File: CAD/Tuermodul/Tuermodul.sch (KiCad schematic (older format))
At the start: 45 parts, among them J101 Conn_02x16_Counter_Clockwise, U101 93LC46B, U102 74HC595, U103 FT4232H, U104 MCP1825S, Y101 12MHz

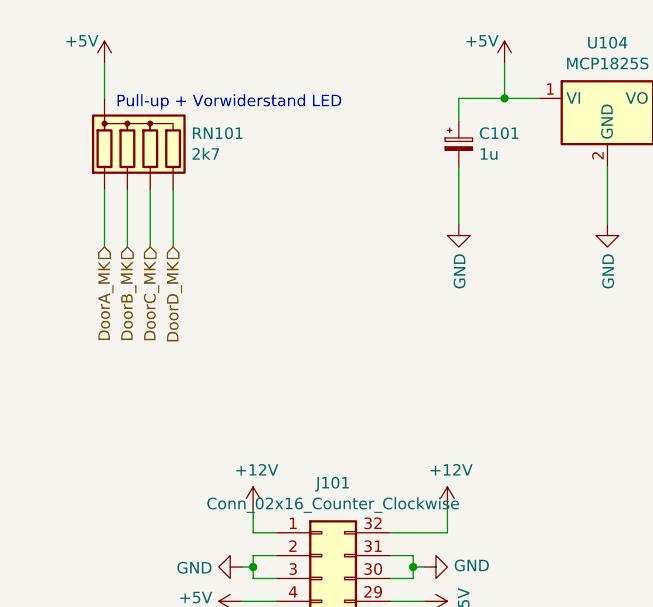
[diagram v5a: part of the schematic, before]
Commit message: -mod: Umbelegung Stecker zwischen Haupt und Frontplatine -add: 100n caps für MK Entprellung -mod: Routing Stecker -mod: Platzierung Front nach Vorgabe
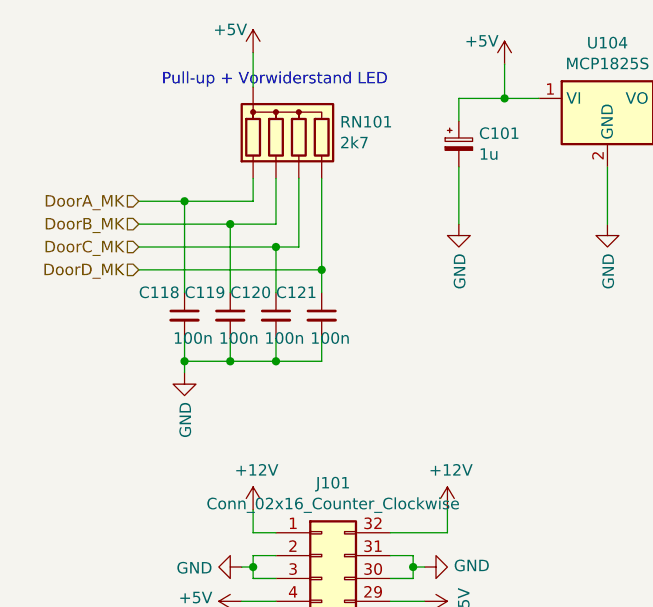
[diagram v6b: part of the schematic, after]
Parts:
- added C118, C119, C120, C121: 100n, Capacitor_SMD:C_0603_1608Metric_Pad1.05x0.95mm_HandSolder, symbol Device:C_Small
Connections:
- net DoorA_MK: now also C118.1
- net DoorB_MK: now also C119.1
- net DoorC_MK: now also C120.1
- net DoorD_MK: now also C121.1
- net GND: now also C118.2, C119.2, C120.2, C121.2
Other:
- moved on the sheet: RN101
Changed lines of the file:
@@
 Wire Wire Line
 	8500 3750 8150 3750
-Text HLabel 800  1450 3    50   Input ~ 0
+Text HLabel 950  1250 0    50   Input ~ 0
 DoorA_MK
-Text HLabel 900  1450 3    50   Input ~ 0
+Text HLabel 950  1350 0    50   Input ~ 0
 DoorB_MK
-Text HLabel 1000 1450 3    50   Input ~ 0
+Text HLabel 950  1450 0    50   Input ~ 0
 DoorC_MK
-Text HLabel 1100 1450 3    50   Input ~ 0
+Text HLabel 950  1550 0    50   Input ~ 0
 DoorD_MK
 $Comp
 L Device:R_Network04 RN101
 U 1 1 5C769116
-P 1000 1000
-F 0 "RN101" H 1180 1046 50  0000 L CNN
-F 1 "2k7" H 1180 955 50  0000 L CNN
-F 2 "Resistor_THT:R_Array_SIP5" V 1275 1000 50  0001 C CNN
-F 3 "http://www.vishay.com/docs/31509/csc.pdf" H 1000 1000 50  0001 C CNN
-	1    1000 1000
+P 1650 950
+F 0 "RN101" H 1830 996 50  0000 L CNN
+F 1 "2k7" H 1830 905 50  0000 L CNN
+F 2 "Resistor_THT:R_Array_SIP5" V 1925 950 50  0001 C CNN
+F 3 "http://www.vishay.com/docs/31509/csc.pdf" H 1650 950 50  0001 C CNN
+	1    1650 950
 	1    0    0    -1
 $EndComp
@@
 L power:+5V #PWR0111
 U 1 1 5C769345
-P 800 650
-F 0 "#PWR0111" H 800 500 50  0001 C CNN
-F 1 "+5V" H 700 750 50  0000 C CNN
-F 2 "" H 800 650 50  0001 C CNN
-F 3 "" H 800 650 50  0001 C CNN
-	1    800  650
-	1    0    0    -1
-$EndComp
-Wire Wire Line
-	800  650  800  800
-Wire Wire Line
-	800  1200 800  1450
-Wire Wire Line
-	900  1200 900  1450
-Wire Wire Line
-	1000 1200 1000 1450
-Wire Wire Line
-	1100 1200 1100 1450
-Text Notes 850  850  0    50   ~ 0
+P 1450 600
+F 0 "#PWR0111" H 1450 450 50  0001 C CNN
+F 1 "+5V" H 1350 700 50  0000 C CNN
+F 2 "" H 1450 600 50  0001 C CNN
+F 3 "" H 1450 600 50  0001 C CNN
+	1    1450 600
+	1    0    0    -1
+$EndComp
+Wire Wire Line
+	1450 600  1450 750
+Text Notes 1050 750  0    50   ~ 0
 Pull-up + Vorwiderstand LED
 Wire Wire Line
@@
 Text HLabel 10400 3200 2    50   Input ~ 0
 ~PWR_EN~
+$Comp
+L Device:C_Small C118
+U 1 1 5CF5F4A8
+P 1150 1750
+F 0 "C118" H 950 1850 50  0000 L CNN
+F 1 "100n" H 1100 1650 50  0000 L CNN
+F 2 "Capacitor_SMD:C_0603_1608Metric_Pad1.05x0.95mm_HandSolder" H 1150 1750 50  0001 C CNN
+F 3 "~" H 1150 1750 50  0001 C CNN
+	1    1150 1750
+	1    0    0    -1
+$EndComp
+$Comp
+L Device:C_Small C119
+U 1 1 5CF5F7BA
+P 1350 1750
+F 0 "C119" H 1150 1850 50  0000 L CNN
+F 1 "100n" H 1300 1650 50  0000 L CNN
+F 2 "Capacitor_SMD:C_0603_1608Metric_Pad1.05x0.95mm_HandSolder" H 1350 1750 50  0001 C CNN
+F 3 "~" H 1350 1750 50  0001 C CNN
+	1    1350 1750
+	1    0    0    -1
+$EndComp
+$Comp
+L Device:C_Small C120
+U 1 1 5CF5F828
+P 1550 1750
+F 0 "C120" H 1350 1850 50  0000 L CNN
+F 1 "100n" H 1500 1650 50  0000 L CNN
+F 2 "Capacitor_SMD:C_0603_1608Metric_Pad1.05x0.95mm_HandSolder" H 1550 1750 50  0001 C CNN
+F 3 "~" H 1550 1750 50  0001 C CNN
+	1    1550 1750
+	1    0    0    -1
+$EndComp
+$Comp
+L Device:C_Small C121
+U 1 1 5CF5F8AA
+P 1750 1750
+F 0 "C121" H 1550 1850 50  0000 L CNN
+F 1 "100n" H 1700 1650 50  0000 L CNN
+F 2 "Capacitor_SMD:C_0603_1608Metric_Pad1.05x0.95mm_HandSolder" H 1750 1750 50  0001 C CNN
+F 3 "~" H 1750 1750 50  0001 C CNN
+	1    1750 1750
+	1    0    0    -1
+$EndComp
+$Comp
+L power:GND #PWR0145
+U 1 1 5CF5FC33
+P 1150 2000
+F 0 "#PWR0145" H 1150 1750 50  0001 C CNN
+F 1 "GND" V 1155 1872 50  0000 R CNN
+F 2 "" H 1150 2000 50  0001 C CNN
+F 3 "" H 1150 2000 50  0001 C CNN
+	1    1150 2000
+	1    0    0    -1
+$EndComp
+Wire Wire Line
+	1150 1950 1150 2000
+Wire Wire Line
+	1450 1250 1450 1150
+Wire Wire Line
+	1550 1350 1550 1150
+Wire Wire Line
+	1650 1450 1650 1150
+Wire Wire Line
+	1750 1550 1750 1150
+Wire Wire Line
+	950  1350 1350 1350
+Wire Wire Line
+	950  1450 1550 1450
+Wire Wire Line
+	950  1550 1750 1550
+Wire Wire Line
+	1750 1850 1750 1950
+Wire Wire Line
+	1550 1850 1550 1950
+Connection ~ 1550 1950
+Wire Wire Line
+	1550 1950 1750 1950
+Wire Wire Line
+	1350 1850 1350 1950
+Connection ~ 1350 1950
+Wire Wire Line
+	1350 1950 1550 1950
+Wire Wire Line
+	1150 1850 1150 1950
+Connection ~ 1150 1950
+Wire Wire Line
+	1150 1950 1350 1950
+Wire Wire Line
+	1750 1650 1750 1550
+Connection ~ 1750 1550
+Wire Wire Line
+	1550 1650 1550 1450
+Connection ~ 1550 1450
+Wire Wire Line
+	1550 1450 1650 1450
+Wire Wire Line
+	1350 1650 1350 1350
+Connection ~ 1350 1350
+Wire Wire Line
+	1350 1350 1550 1350
+Wire Wire Line
+	950  1250 1150 1250
+Wire Wire Line
+	1150 1650 1150 1250
+Connection ~ 1150 1250
+Wire Wire Line
+	1150 1250 1450 1250
 $EndSCHEMATC

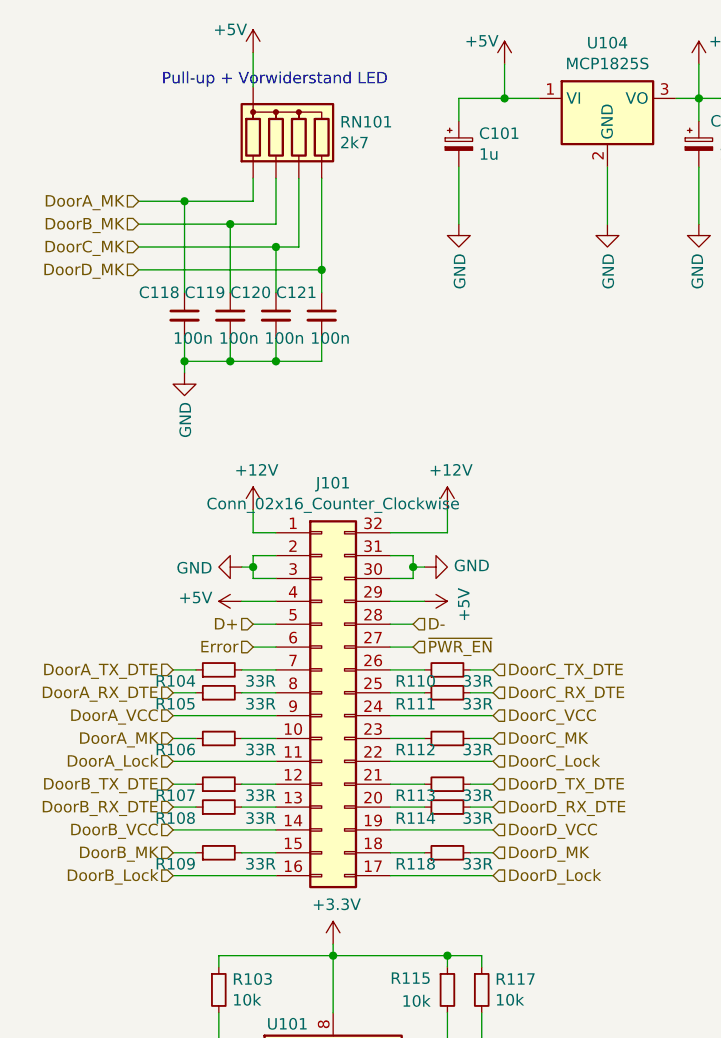
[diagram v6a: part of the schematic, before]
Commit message: -mod: Änderungen aus Review in Schaltplan und Layout
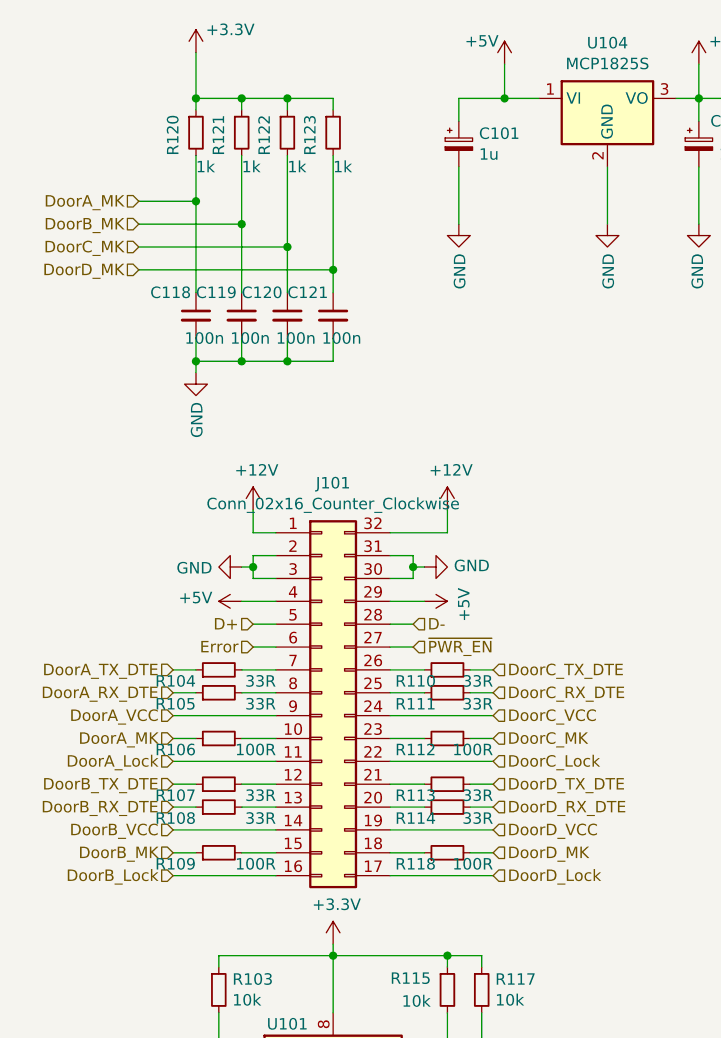
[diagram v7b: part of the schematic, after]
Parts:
- removed RN101: 2k7, Resistor_THT:R_Array_SIP5, symbol Device:R_Network04
- added R120, R121, R122, R123: 1k, Resistor_SMD:R_0603_1608Metric_Pad1.05x0.95mm_HandSolder, symbol Device:R_Small
- R106, R109, R112, R118: value 33R -> 100R
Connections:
- net +3V3: now also R120.1, R121.1, R122.1, R123.1
- net DoorA_MK: now also R120.2
- net DoorB_MK: now also R121.2
- net DoorC_MK: now also R122.2
- net DoorD_MK: now also R123.2
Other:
- note removed: "Pull-up + Vorwiderstand LED"
- moved on the sheet: C118, C119, C120, C121
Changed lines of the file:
@@
 Text HLabel 950  1550 0    50   Input ~ 0
 DoorD_MK
-$Comp
-L Device:R_Network04 RN101
-U 1 1 5C769116
-P 1650 950
-F 0 "RN101" H 1830 996 50  0000 L CNN
-F 1 "2k7" H 1830 905 50  0000 L CNN
-F 2 "Resistor_THT:R_Array_SIP5" V 1925 950 50  0001 C CNN
-F 3 "http://www.vishay.com/docs/31509/csc.pdf" H 1650 950 50  0001 C CNN
-	1    1650 950
-	1    0    0    -1
-$EndComp
-$Comp
-L power:+5V #PWR0111
-U 1 1 5C769345
-P 1450 600
-F 0 "#PWR0111" H 1450 450 50  0001 C CNN
-F 1 "+5V" H 1350 700 50  0000 C CNN
-F 2 "" H 1450 600 50  0001 C CNN
-F 3 "" H 1450 600 50  0001 C CNN
-	1    1450 600
-	1    0    0    -1
-$EndComp
-Wire Wire Line
-	1450 600  1450 750
-Text Notes 1050 750  0    50   ~ 0
-Pull-up + Vorwiderstand LED
 Wire Wire Line
 	7100 2200 6950 2200
@@
 P 1300 3600
 F 0 "R106" V 1250 3700 50  0000 L CNN
-F 1 "33R" V 1250 3350 50  0000 L CNN
+F 1 "100R" V 1250 3350 50  0000 L CNN
 F 2 "Resistor_SMD:R_0603_1608Metric_Pad1.05x0.95mm_HandSolder" H 1300 3600 50  0001 C CNN
 F 3 "~" H 1300 3600 50  0001 C CNN
@@
 P 1300 4100
 F 0 "R109" V 1250 4200 50  0000 L CNN
-F 1 "33R" V 1250 3850 50  0000 L CNN
+F 1 "100R" V 1250 3850 50  0000 L CNN
 F 2 "Resistor_SMD:R_0603_1608Metric_Pad1.05x0.95mm_HandSolder" H 1300 4100 50  0001 C CNN
 F 3 "~" H 1300 4100 50  0001 C CNN
@@
 P 2300 4100
 F 0 "R118" V 2250 4150 50  0000 L CNN
-F 1 "33R" V 2250 3900 50  0000 L CNN
+F 1 "100R" V 2250 3900 50  0000 L CNN
 F 2 "Resistor_SMD:R_0603_1608Metric_Pad1.05x0.95mm_HandSolder" H 2300 4100 50  0001 C CNN
 F 3 "~" H 2300 4100 50  0001 C CNN
@@
 P 2300 3600
 F 0 "R112" V 2250 3650 50  0000 L CNN
-F 1 "33R" V 2250 3400 50  0000 L CNN
+F 1 "100R" V 2250 3400 50  0000 L CNN
 F 2 "Resistor_SMD:R_0603_1608Metric_Pad1.05x0.95mm_HandSolder" H 2300 3600 50  0001 C CNN
 F 3 "~" H 2300 3600 50  0001 C CNN
@@
 L Device:C_Small C118
 U 1 1 5CF5F4A8
-P 1150 1750
-F 0 "C118" H 950 1850 50  0000 L CNN
-F 1 "100n" H 1100 1650 50  0000 L CNN
-F 2 "Capacitor_SMD:C_0603_1608Metric_Pad1.05x0.95mm_HandSolder" H 1150 1750 50  0001 C CNN
-F 3 "~" H 1150 1750 50  0001 C CNN
-	1    1150 1750
+P 1200 1750
+F 0 "C118" H 1000 1850 50  0000 L CNN
+F 1 "100n" H 1150 1650 50  0000 L CNN
+F 2 "Capacitor_SMD:C_0603_1608Metric_Pad1.05x0.95mm_HandSolder" H 1200 1750 50  0001 C CNN
+F 3 "~" H 1200 1750 50  0001 C CNN
+	1    1200 1750
 	1    0    0    -1
 $EndComp
@@
 L Device:C_Small C119
 U 1 1 5CF5F7BA
-P 1350 1750
-F 0 "C119" H 1150 1850 50  0000 L CNN
-F 1 "100n" H 1300 1650 50  0000 L CNN
-F 2 "Capacitor_SMD:C_0603_1608Metric_Pad1.05x0.95mm_HandSolder" H 1350 1750 50  0001 C CNN
-F 3 "~" H 1350 1750 50  0001 C CNN
-	1    1350 1750
+P 1400 1750
+F 0 "C119" H 1200 1850 50  0000 L CNN
+F 1 "100n" H 1350 1650 50  0000 L CNN
+F 2 "Capacitor_SMD:C_0603_1608Metric_Pad1.05x0.95mm_HandSolder" H 1400 1750 50  0001 C CNN
+F 3 "~" H 1400 1750 50  0001 C CNN
+	1    1400 1750
 	1    0    0    -1
 $EndComp
@@
 L Device:C_Small C120
 U 1 1 5CF5F828
-P 1550 1750
-F 0 "C120" H 1350 1850 50  0000 L CNN
-F 1 "100n" H 1500 1650 50  0000 L CNN
-F 2 "Capacitor_SMD:C_0603_1608Metric_Pad1.05x0.95mm_HandSolder" H 1550 1750 50  0001 C CNN
-F 3 "~" H 1550 1750 50  0001 C CNN
-	1    1550 1750
+P 1600 1750
+F 0 "C120" H 1400 1850 50  0000 L CNN
+F 1 "100n" H 1550 1650 50  0000 L CNN
+F 2 "Capacitor_SMD:C_0603_1608Metric_Pad1.05x0.95mm_HandSolder" H 1600 1750 50  0001 C CNN
+F 3 "~" H 1600 1750 50  0001 C CNN
+	1    1600 1750
 	1    0    0    -1
 $EndComp
@@
 L Device:C_Small C121
 U 1 1 5CF5F8AA
-P 1750 1750
-F 0 "C121" H 1550 1850 50  0000 L CNN
-F 1 "100n" H 1700 1650 50  0000 L CNN
-F 2 "Capacitor_SMD:C_0603_1608Metric_Pad1.05x0.95mm_HandSolder" H 1750 1750 50  0001 C CNN
-F 3 "~" H 1750 1750 50  0001 C CNN
-	1    1750 1750
+P 1800 1750
+F 0 "C121" H 1600 1850 50  0000 L CNN
+F 1 "100n" H 1750 1650 50  0000 L CNN
+F 2 "Capacitor_SMD:C_0603_1608Metric_Pad1.05x0.95mm_HandSolder" H 1800 1750 50  0001 C CNN
+F 3 "~" H 1800 1750 50  0001 C CNN
+	1    1800 1750
 	1    0    0    -1
 $EndComp
@@
 L power:GND #PWR0145
 U 1 1 5CF5FC33
-P 1150 2000
-F 0 "#PWR0145" H 1150 1750 50  0001 C CNN
-F 1 "GND" V 1155 1872 50  0000 R CNN
-F 2 "" H 1150 2000 50  0001 C CNN
-F 3 "" H 1150 2000 50  0001 C CNN
-	1    1150 2000
-	1    0    0    -1
-$EndComp
-Wire Wire Line
-	1150 1950 1150 2000
-Wire Wire Line
-	1450 1250 1450 1150
-Wire Wire Line
-	1550 1350 1550 1150
-Wire Wire Line
-	1650 1450 1650 1150
-Wire Wire Line
-	1750 1550 1750 1150
-Wire Wire Line
-	950  1350 1350 1350
-Wire Wire Line
-	950  1450 1550 1450
-Wire Wire Line
-	950  1550 1750 1550
-Wire Wire Line
-	1750 1850 1750 1950
-Wire Wire Line
-	1550 1850 1550 1950
-Connection ~ 1550 1950
-Wire Wire Line
-	1550 1950 1750 1950
-Wire Wire Line
-	1350 1850 1350 1950
-Connection ~ 1350 1950
-Wire Wire Line
-	1350 1950 1550 1950
-Wire Wire Line
-	1150 1850 1150 1950
-Connection ~ 1150 1950
-Wire Wire Line
-	1150 1950 1350 1950
-Wire Wire Line
-	1750 1650 1750 1550
-Connection ~ 1750 1550
-Wire Wire Line
-	1550 1650 1550 1450
-Connection ~ 1550 1450
-Wire Wire Line
-	1550 1450 1650 1450
-Wire Wire Line
-	1350 1650 1350 1350
-Connection ~ 1350 1350
-Wire Wire Line
-	1350 1350 1550 1350
-Wire Wire Line
-	950  1250 1150 1250
-Wire Wire Line
-	1150 1650 1150 1250
-Connection ~ 1150 1250
-Wire Wire Line
-	1150 1250 1450 1250
+P 1200 2000
+F 0 "#PWR0145" H 1200 1750 50  0001 C CNN
+F 1 "GND" V 1205 1872 50  0000 R CNN
+F 2 "" H 1200 2000 50  0001 C CNN
+F 3 "" H 1200 2000 50  0001 C CNN
+	1    1200 2000
+	1    0    0    -1
+$EndComp
+Wire Wire Line
+	1200 1950 1200 2000
+Wire Wire Line
+	950  1350 1400 1350
+Wire Wire Line
+	950  1450 1600 1450
+Wire Wire Line
+	950  1550 1800 1550
+Wire Wire Line
+	1800 1850 1800 1950
+Wire Wire Line
+	1600 1850 1600 1950
+Connection ~ 1600 1950
+Wire Wire Line
+	1600 1950 1800 1950
+Wire Wire Line
+	1400 1850 1400 1950
+Connection ~ 1400 1950
+Wire Wire Line
+	1400 1950 1600 1950
+Wire Wire Line
+	1200 1850 1200 1950
+Connection ~ 1200 1950
+Wire Wire Line
+	1200 1950 1400 1950
+Wire Wire Line
+	1800 1650 1800 1550
+Connection ~ 1800 1550
+Wire Wire Line
+	1600 1650 1600 1450
+Connection ~ 1600 1450
+Wire Wire Line
+	1400 1650 1400 1350
+Connection ~ 1400 1350
+Wire Wire Line
+	950  1250 1200 1250
+Wire Wire Line
+	1200 1650 1200 1250
+Connection ~ 1200 1250
+$Comp
+L Device:R_Small R120
+U 1 1 5C9988EB
+P 1200 950
+F 0 "R120" V 1100 850 50  0000 L CNN
+F 1 "1k" H 1200 800 50  0000 L CNN
+F 2 "Resistor_SMD:R_0603_1608Metric_Pad1.05x0.95mm_HandSolder" H 1200 950 50  0001 C CNN
+F 3 "~" H 1200 950 50  0001 C CNN
+	1    1200 950
+	1    0    0    -1
+$EndComp
+$Comp
+L Device:R_Small R121
+U 1 1 5C999088
+P 1400 950
+F 0 "R121" V 1300 850 50  0000 L CNN
+F 1 "1k" H 1400 800 50  0000 L CNN
+F 2 "Resistor_SMD:R_0603_1608Metric_Pad1.05x0.95mm_HandSolder" H 1400 950 50  0001 C CNN
+F 3 "~" H 1400 950 50  0001 C CNN
+	1    1400 950
+	1    0    0    -1
+$EndComp
+$Comp
+L Device:R_Small R122
+U 1 1 5C9990FC
+P 1600 950
+F 0 "R122" V 1500 850 50  0000 L CNN
+F 1 "1k" H 1600 800 50  0000 L CNN
+F 2 "Resistor_SMD:R_0603_1608Metric_Pad1.05x0.95mm_HandSolder" H 1600 950 50  0001 C CNN
+F 3 "~" H 1600 950 50  0001 C CNN
+	1    1600 950
+	1    0    0    -1
+$EndComp
+$Comp
+L Device:R_Small R123
+U 1 1 5C999172
+P 1800 950
+F 0 "R123" V 1700 850 50  0000 L CNN
+F 1 "1k" H 1800 800 50  0000 L CNN
+F 2 "Resistor_SMD:R_0603_1608Metric_Pad1.05x0.95mm_HandSolder" H 1800 950 50  0001 C CNN
+F 3 "~" H 1800 950 50  0001 C CNN
+	1    1800 950
+	1    0    0    -1
+$EndComp
+Wire Wire Line
+	1200 800  1400 800
+Wire Wire Line
+	1800 800  1800 850
+Wire Wire Line
+	1200 600  1200 800
+Wire Wire Line
+	1600 850  1600 800
+Connection ~ 1600 800
+Wire Wire Line
+	1600 800  1800 800
+Wire Wire Line
+	1400 850  1400 800
+Connection ~ 1400 800
+Wire Wire Line
+	1400 800  1600 800
+Wire Wire Line
+	1200 850  1200 800
+Connection ~ 1200 800
+Wire Wire Line
+	1200 1050 1200 1250
+Wire Wire Line
+	1400 1050 1400 1350
+Wire Wire Line
+	1600 1050 1600 1450
+Wire Wire Line
+	1800 1050 1800 1550
+$Comp
+L power:+3.3V #PWR0111
+U 1 1 5CDBD7A1
+P 1200 600
+F 0 "#PWR0111" H 1200 450 50  0001 C CNN
+F 1 "+3.3V" H 1350 700 50  0000 C CNN
+F 2 "" H 1200 600 50  0001 C CNN
+F 3 "" H 1200 600 50  0001 C CNN
+	1    1200 600
+	1    0    0    -1
+$EndComp
 $EndSCHEMATC

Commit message: -mod: DIN Stecker auf Typ D geändert. Layout angepasst und optimiert.
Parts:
- J101: footprint DIN41612_Connectors_custom:DIN41612_B_2x16_Horizontal_counter_clockwise -> DIN41612_Connectors_custom:DIN41612_D_32pol_90deg
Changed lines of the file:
@@
 F 0 "J101" H 1800 4317 50  0000 C CNN
 F 1 "Conn_02x16_Counter_Clockwise" H 1800 4226 50  0000 C CNN
-F 2 "DIN41612_Connectors_custom:DIN41612_B_2x16_Horizontal_counter_clockwise" H 1750 3400 50  0001 C CNN
+F 2 "DIN41612_Connectors_custom:DIN41612_D_32pol_90deg" H 1750 3400 50  0001 C CNN
 F 3 "~" H 1750 3400 50  0001 C CNN
 	1    1750 3400
